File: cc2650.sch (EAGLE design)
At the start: 23 parts, among them IC4 CC2650MODAMOHR, SW1 SPST_TACT-KMR2, SW2 SPST_TACT-KMR2, U402 TPS62237DRY

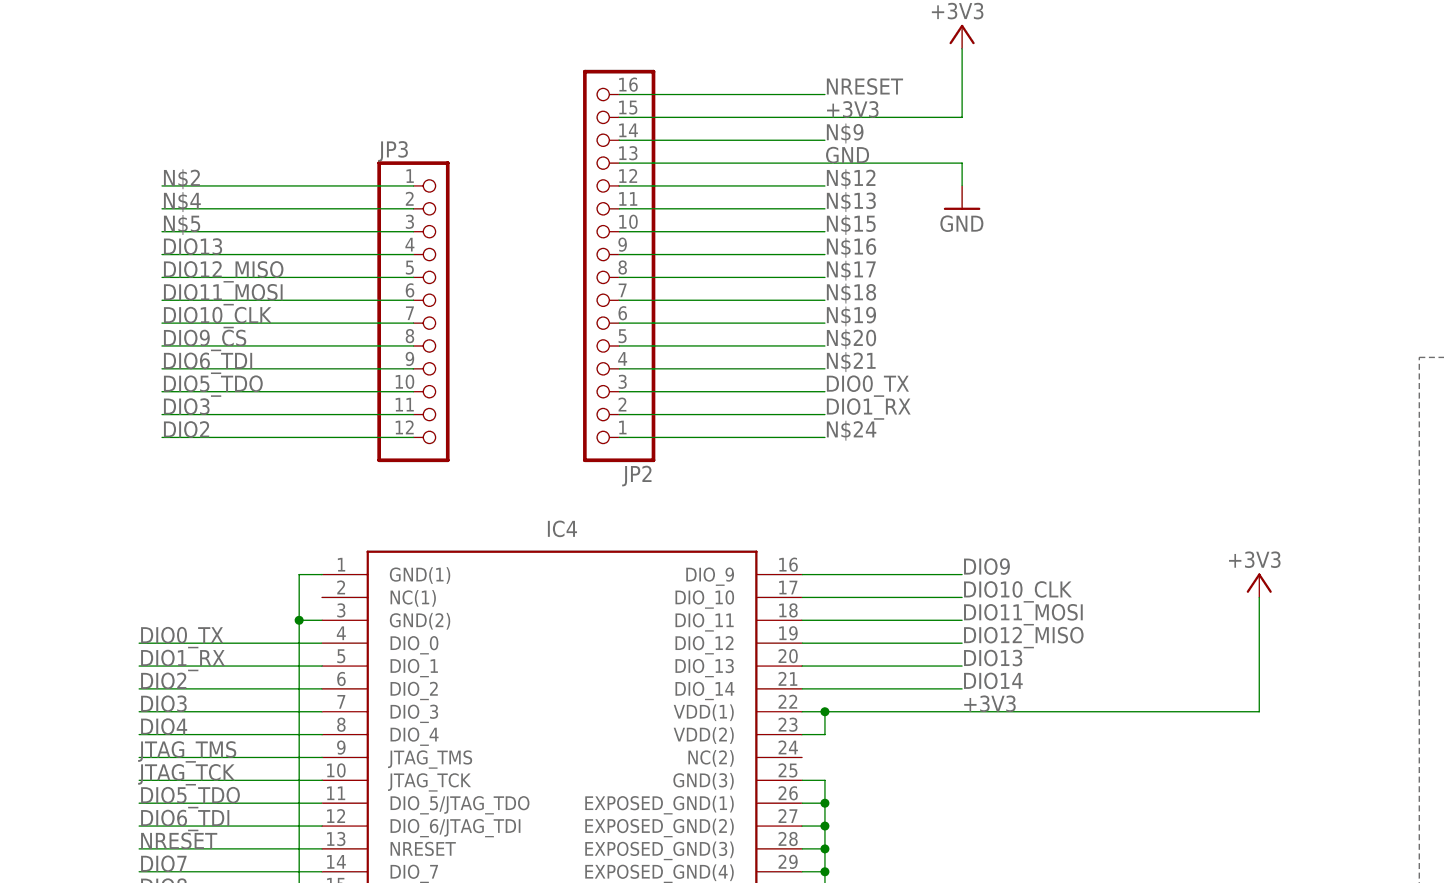
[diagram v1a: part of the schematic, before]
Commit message: changed pinout.
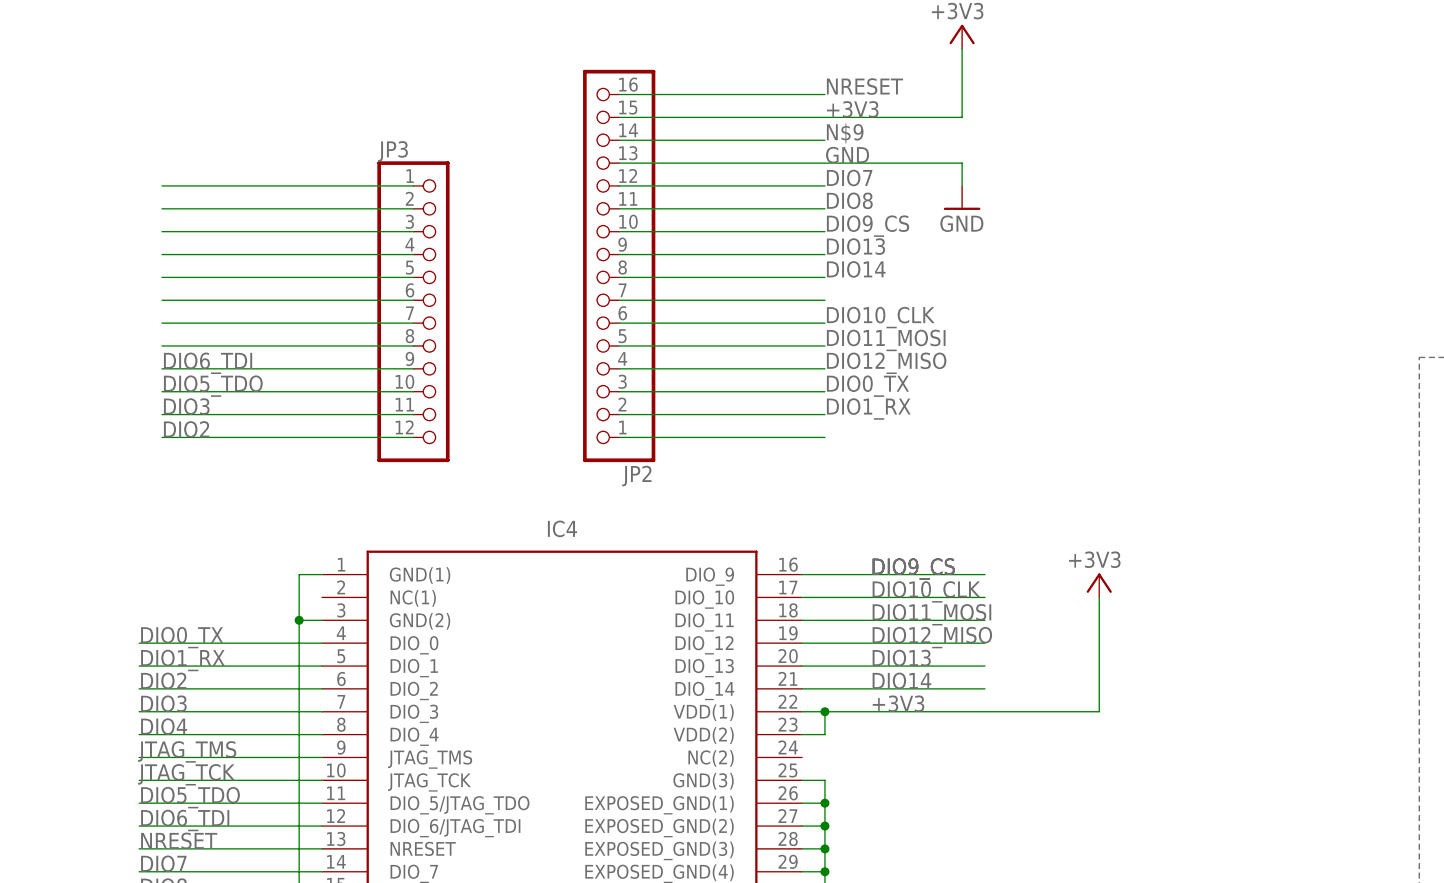
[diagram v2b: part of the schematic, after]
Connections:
- removed net DIO9: IC4.DIO_9
- removed net N$1: IC4.DIO_10
- removed net N$12: JP2.12
- removed net N$13: JP2.11
- removed net N$15: JP2.10
- removed net N$16: JP2.9
- removed net N$17: JP2.8
- removed net N$19: JP2.6
- removed net N$20: JP2.5
- removed net N$21: JP2.4
- net DIO10_CLK: now also IC4.DIO_10, JP2.6
- net DIO11_MOSI: now also JP2.5
- net DIO12_MISO: now also JP2.4
- net DIO13: now also JP2.9
- net DIO14: now also JP2.8
- net DIO7: now also JP2.12
- net DIO8: now also JP2.11
- net DIO9_CS: now also IC4.DIO_9, JP2.10
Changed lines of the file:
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@@
 <instance part="D1" gate="G$1" x="53.34" y="-10.16" rot="R90"/>
 <instance part="GND4" gate="1" x="35.56" y="-30.48"/>
-<instance part="+3V6" gate="G$1" x="0" y="7.62" smashed="yes">
-<attribute name="VALUE" x="2.54" y="10.16" size="1.778" layer="96" rot="R180"/>
+<instance part="+3V6" gate="G$1" x="-17.78" y="7.62" smashed="yes">
+<attribute name="VALUE" x="-15.24" y="10.16" size="1.778" layer="96" rot="R180"/>
 </instance>
 <instance part="GND5" gate="1" x="93.98" y="-76.2"/>
@@
 <segment>
 <pinref part="+3V6" gate="G$1" pin="+3V3"/>
-<wire x1="0" y1="5.08" x2="0" y2="-7.62" width="0.1524" layer="91"/>
+<wire x1="-17.78" y1="5.08" x2="-17.78" y2="-7.62" width="0.1524" layer="91"/>
 <pinref part="IC4" gate="G$1" pin="VDD(1)"/>
-<wire x1="0" y1="-7.62" x2="-48.26" y2="-7.62" width="0.1524" layer="91"/>
+<wire x1="-17.78" y1="-7.62" x2="-48.26" y2="-7.62" width="0.1524" layer="91"/>
 <pinref part="IC4" gate="G$1" pin="VDD(2)"/>
 <wire x1="-48.26" y1="-7.62" x2="-50.8" y2="-7.62" width="0.1524" layer="91"/>
@@
 <wire x1="-48.26" y1="-10.16" x2="-48.26" y2="-7.62" width="0.1524" layer="91"/>
 <junction x="-48.26" y="-7.62"/>
-<label x="-33.02" y="-7.62" size="1.778" layer="95"/>
+<label x="-43.18" y="-7.62" size="1.778" layer="95"/>
 </segment>
 <segment>
@@
 <label x="-124.46" y="-25.4" size="1.778" layer="95"/>
 </segment>
+<segment>
+<pinref part="JP2" gate="A" pin="12"/>
+<wire x1="-71.12" y1="50.8" x2="-48.26" y2="50.8" width="0.1524" layer="91"/>
+<label x="-48.26" y="50.8" size="1.778" layer="95"/>
+</segment>
 </net>
 <net name="DIO0_TX" class="0">
@@
 <net name="DIO10_CLK" class="0">
 <segment>
-<label x="-33.02" y="5.08" size="1.778" layer="95"/>
-</segment>
-<segment>
 <pinref part="JP3" gate="G$1" pin="7"/>
 <wire x1="-93.98" y1="35.56" x2="-121.92" y2="35.56" width="0.1524" layer="91"/>
-<label x="-121.92" y="35.56" size="1.778" layer="95"/>
+</segment>
+<segment>
+<pinref part="IC4" gate="G$1" pin="DIO_10"/>
+<wire x1="-50.8" y1="5.08" x2="-30.48" y2="5.08" width="0.1524" layer="91"/>
+<label x="-43.18" y="5.08" size="1.778" layer="95"/>
+</segment>
+<segment>
+<pinref part="JP2" gate="A" pin="6"/>
+<wire x1="-71.12" y1="35.56" x2="-48.26" y2="35.56" width="0.1524" layer="91"/>
+<label x="-48.26" y="35.56" size="1.778" layer="95"/>
 </segment>
 </net>
@@
 <pinref part="JP3" gate="G$1" pin="8"/>
 <wire x1="-93.98" y1="33.02" x2="-121.92" y2="33.02" width="0.1524" layer="91"/>
-<label x="-121.92" y="33.02" size="1.778" layer="95"/>
+</segment>
+<segment>
+<pinref part="IC4" gate="G$1" pin="DIO_9"/>
+<wire x1="-50.8" y1="7.62" x2="-30.48" y2="7.62" width="0.1524" layer="91"/>
+<label x="-43.18" y="7.62" size="1.778" layer="95"/>
+<label x="-43.18" y="7.62" size="1.778" layer="95"/>
+</segment>
+<segment>
+<pinref part="JP2" gate="A" pin="10"/>
+<wire x1="-71.12" y1="45.72" x2="-48.26" y2="45.72" width="0.1524" layer="91"/>
+<label x="-48.26" y="45.72" size="1.778" layer="95"/>
 </segment>
 </net>
@@
 <segment>
 <pinref part="IC4" gate="G$1" pin="DIO_12"/>
-<wire x1="-33.02" y1="0" x2="-50.8" y2="0" width="0.1524" layer="91"/>
-<label x="-33.02" y="0" size="1.778" layer="95"/>
+<wire x1="-30.48" y1="0" x2="-50.8" y2="0" width="0.1524" layer="91"/>
+<label x="-43.18" y="0" size="1.778" layer="95"/>
 </segment>
 <segment>
 <pinref part="JP3" gate="G$1" pin="5"/>
 <wire x1="-93.98" y1="40.64" x2="-121.92" y2="40.64" width="0.1524" layer="91"/>
-<label x="-121.92" y="40.64" size="1.778" layer="95"/>
+</segment>
+<segment>
+<pinref part="JP2" gate="A" pin="4"/>
+<wire x1="-71.12" y1="30.48" x2="-48.26" y2="30.48" width="0.1524" layer="91"/>
+<label x="-48.26" y="30.48" size="1.778" layer="95"/>
 </segment>
 </net>
@@
 <segment>
 <pinref part="IC4" gate="G$1" pin="DIO_13"/>
-<wire x1="-50.8" y1="-2.54" x2="-33.02" y2="-2.54" width="0.1524" layer="91"/>
-<label x="-33.02" y="-2.54" size="1.778" layer="95"/>
+<wire x1="-50.8" y1="-2.54" x2="-30.48" y2="-2.54" width="0.1524" layer="91"/>
+<label x="-43.18" y="-2.54" size="1.778" layer="95"/>
 </segment>
 <segment>
 <pinref part="JP3" gate="G$1" pin="4"/>
 <wire x1="-93.98" y1="43.18" x2="-121.92" y2="43.18" width="0.1524" layer="91"/>
-<label x="-121.92" y="43.18" size="1.778" layer="95"/>
+</segment>
+<segment>
+<pinref part="JP2" gate="A" pin="9"/>
+<wire x1="-71.12" y1="43.18" x2="-48.26" y2="43.18" width="0.1524" layer="91"/>
+<label x="-48.26" y="43.18" size="1.778" layer="95"/>
 </segment>
 </net>
@@
 <segment>
 <pinref part="IC4" gate="G$1" pin="DIO_14"/>
-<wire x1="-33.02" y1="-5.08" x2="-50.8" y2="-5.08" width="0.1524" layer="91"/>
-<label x="-33.02" y="-5.08" size="1.778" layer="95"/>
+<wire x1="-30.48" y1="-5.08" x2="-50.8" y2="-5.08" width="0.1524" layer="91"/>
+<label x="-43.18" y="-5.08" size="1.778" layer="95"/>
+</segment>
+<segment>
+<pinref part="JP2" gate="A" pin="8"/>
+<wire x1="-71.12" y1="40.64" x2="-48.26" y2="40.64" width="0.1524" layer="91"/>
+<label x="-48.26" y="40.64" size="1.778" layer="95"/>
 </segment>
 </net>
@@
 </segment>
 </net>
-<net name="N$1" class="0">
-<segment>
-<pinref part="IC4" gate="G$1" pin="DIO_10"/>
-<wire x1="-50.8" y1="5.08" x2="-33.02" y2="5.08" width="0.1524" layer="91"/>
-</segment>
-</net>
 <net name="DIO11_MOSI" class="0">
 <segment>
 <pinref part="IC4" gate="G$1" pin="DIO_11"/>
-<wire x1="-33.02" y1="2.54" x2="-50.8" y2="2.54" width="0.1524" layer="91"/>
-<label x="-33.02" y="2.54" size="1.778" layer="95"/>
+<wire x1="-30.48" y1="2.54" x2="-50.8" y2="2.54" width="0.1524" layer="91"/>
+<label x="-43.18" y="2.54" size="1.778" layer="95"/>
 </segment>
 <segment>
 <pinref part="JP3" gate="G$1" pin="6"/>
 <wire x1="-93.98" y1="38.1" x2="-121.92" y2="38.1" width="0.1524" layer="91"/>
-<label x="-121.92" y="38.1" size="1.778" layer="95"/>
-</segment>
-</net>
-<net name="DIO9" class="0">
-<segment>
-<pinref part="IC4" gate="G$1" pin="DIO_9"/>
-<wire x1="-50.8" y1="7.62" x2="-33.02" y2="7.62" width="0.1524" layer="91"/>
-<label x="-33.02" y="7.62" size="1.778" layer="95"/>
+</segment>
+<segment>
+<pinref part="JP2" gate="A" pin="5"/>
+<wire x1="-71.12" y1="33.02" x2="-48.26" y2="33.02" width="0.1524" layer="91"/>
+<label x="-48.26" y="33.02" size="1.778" layer="95"/>
 </segment>
 </net>
@@
 <pinref part="JP3" gate="G$1" pin="1"/>
 <wire x1="-93.98" y1="50.8" x2="-121.92" y2="50.8" width="0.1524" layer="91"/>
-<label x="-121.92" y="50.8" size="1.778" layer="95"/>
 </segment>
 </net>
@@
 <pinref part="JP3" gate="G$1" pin="2"/>
 <wire x1="-93.98" y1="48.26" x2="-121.92" y2="48.26" width="0.1524" layer="91"/>
-<label x="-121.92" y="48.26" size="1.778" layer="95"/>
 </segment>
 </net>
@@
 <pinref part="JP3" gate="G$1" pin="3"/>
 <wire x1="-93.98" y1="45.72" x2="-121.92" y2="45.72" width="0.1524" layer="91"/>
-<label x="-121.92" y="45.72" size="1.778" layer="95"/>
 </segment>
 </net>
@@
 <label x="-124.46" y="-27.94" size="1.778" layer="95"/>
 </segment>
+<segment>
+<pinref part="JP2" gate="A" pin="11"/>
+<wire x1="-71.12" y1="48.26" x2="-48.26" y2="48.26" width="0.1524" layer="91"/>
+<label x="-48.26" y="48.26" size="1.778" layer="95"/>
+</segment>
 </net>
 <net name="N$9" class="0">
@@
 </segment>
 </net>
-<net name="N$12" class="0">
-<segment>
-<pinref part="JP2" gate="A" pin="12"/>
-<wire x1="-71.12" y1="50.8" x2="-48.26" y2="50.8" width="0.1524" layer="91"/>
-<label x="-48.26" y="50.8" size="1.778" layer="95"/>
-</segment>
-</net>
-<net name="N$13" class="0">
-<segment>
-<pinref part="JP2" gate="A" pin="11"/>
-<wire x1="-71.12" y1="48.26" x2="-48.26" y2="48.26" width="0.1524" layer="91"/>
-<label x="-48.26" y="48.26" size="1.778" layer="95"/>
-</segment>
-</net>
-<net name="N$15" class="0">
-<segment>
-<pinref part="JP2" gate="A" pin="10"/>
-<wire x1="-71.12" y1="45.72" x2="-48.26" y2="45.72" width="0.1524" layer="91"/>
-<label x="-48.26" y="45.72" size="1.778" layer="95"/>
-</segment>
-</net>
-<net name="N$16" class="0">
-<segment>
-<pinref part="JP2" gate="A" pin="9"/>
-<wire x1="-71.12" y1="43.18" x2="-48.26" y2="43.18" width="0.1524" layer="91"/>
-<label x="-48.26" y="43.18" size="1.778" layer="95"/>
-</segment>
-</net>
-<net name="N$17" class="0">
-<segment>
-<pinref part="JP2" gate="A" pin="8"/>
-<wire x1="-71.12" y1="40.64" x2="-48.26" y2="40.64" width="0.1524" layer="91"/>
-<label x="-48.26" y="40.64" size="1.778" layer="95"/>
-</segment>
-</net>
 <net name="N$18" class="0">
 <segment>
 <pinref part="JP2" gate="A" pin="7"/>
 <wire x1="-71.12" y1="38.1" x2="-48.26" y2="38.1" width="0.1524" layer="91"/>
-<label x="-48.26" y="38.1" size="1.778" layer="95"/>
-</segment>
-</net>
-<net name="N$19" class="0">
-<segment>
-<pinref part="JP2" gate="A" pin="6"/>
-<wire x1="-71.12" y1="35.56" x2="-48.26" y2="35.56" width="0.1524" layer="91"/>
-<label x="-48.26" y="35.56" size="1.778" layer="95"/>
-</segment>
-</net>
-<net name="N$20" class="0">
-<segment>
-<pinref part="JP2" gate="A" pin="5"/>
-<wire x1="-71.12" y1="33.02" x2="-48.26" y2="33.02" width="0.1524" layer="91"/>
-<label x="-48.26" y="33.02" size="1.778" layer="95"/>
-</segment>
-</net>
-<net name="N$21" class="0">
-<segment>
-<pinref part="JP2" gate="A" pin="4"/>
-<wire x1="-71.12" y1="30.48" x2="-48.26" y2="30.48" width="0.1524" layer="91"/>
-<label x="-48.26" y="30.48" size="1.778" layer="95"/>
 </segment>
 </net>
@@
 <pinref part="JP2" gate="A" pin="1"/>
 <wire x1="-71.12" y1="22.86" x2="-48.26" y2="22.86" width="0.1524" layer="91"/>
-<label x="-48.26" y="22.86" size="1.778" layer="95"/>
-</segment>
-</net>
+</segment>
+</net>

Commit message: changed pinout and added second routing path.
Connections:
- removed net N$18: JP2.7
- removed net N$2: JP3.1
- removed net N$24: JP2.1
- removed net N$4: JP3.2
- removed net N$5: JP3.3
- removed net N$9: JP2.14
- net DIO10_CLK: no longer JP3.7
- net DIO11_MOSI: no longer JP3.6
- net DIO12_MISO: no longer JP3.5
- net DIO13: no longer JP3.4
- net DIO9_CS: no longer JP3.8
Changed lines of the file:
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@@
 <net name="DIO10_CLK" class="0">
-<segment>
-<pinref part="JP3" gate="G$1" pin="7"/>
-<wire x1="-93.98" y1="35.56" x2="-121.92" y2="35.56" width="0.1524" layer="91"/>
-</segment>
 <segment>
 <pinref part="IC4" gate="G$1" pin="DIO_10"/>
@@
 <net name="DIO9_CS" class="0">
 <segment>
-<pinref part="JP3" gate="G$1" pin="8"/>
-<wire x1="-93.98" y1="33.02" x2="-121.92" y2="33.02" width="0.1524" layer="91"/>
-</segment>
-<segment>
 <pinref part="IC4" gate="G$1" pin="DIO_9"/>
 <wire x1="-50.8" y1="7.62" x2="-30.48" y2="7.62" width="0.1524" layer="91"/>
@@
 </segment>
 <segment>
-<pinref part="JP3" gate="G$1" pin="5"/>
-<wire x1="-93.98" y1="40.64" x2="-121.92" y2="40.64" width="0.1524" layer="91"/>
-</segment>
-<segment>
 <pinref part="JP2" gate="A" pin="4"/>
 <wire x1="-71.12" y1="30.48" x2="-48.26" y2="30.48" width="0.1524" layer="91"/>
@@
 <wire x1="-50.8" y1="-2.54" x2="-30.48" y2="-2.54" width="0.1524" layer="91"/>
 <label x="-43.18" y="-2.54" size="1.778" layer="95"/>
-</segment>
-<segment>
-<pinref part="JP3" gate="G$1" pin="4"/>
-<wire x1="-93.98" y1="43.18" x2="-121.92" y2="43.18" width="0.1524" layer="91"/>
 </segment>
 <segment>
@@
 </segment>
 <segment>
-<pinref part="JP3" gate="G$1" pin="6"/>
-<wire x1="-93.98" y1="38.1" x2="-121.92" y2="38.1" width="0.1524" layer="91"/>
-</segment>
-<segment>
 <pinref part="JP2" gate="A" pin="5"/>
 <wire x1="-71.12" y1="33.02" x2="-48.26" y2="33.02" width="0.1524" layer="91"/>
 <label x="-48.26" y="33.02" size="1.778" layer="95"/>
-</segment>
-</net>
-<net name="N$2" class="0">
-<segment>
-<pinref part="JP3" gate="G$1" pin="1"/>
-<wire x1="-93.98" y1="50.8" x2="-121.92" y2="50.8" width="0.1524" layer="91"/>
-</segment>
-</net>
-<net name="N$4" class="0">
-<segment>
-<pinref part="JP3" gate="G$1" pin="2"/>
-<wire x1="-93.98" y1="48.26" x2="-121.92" y2="48.26" width="0.1524" layer="91"/>
-</segment>
-</net>
-<net name="N$5" class="0">
-<segment>
-<pinref part="JP3" gate="G$1" pin="3"/>
-<wire x1="-93.98" y1="45.72" x2="-121.92" y2="45.72" width="0.1524" layer="91"/>
 </segment>
 </net>
@@
 </segment>
 </net>
-<net name="N$9" class="0">
-<segment>
-<pinref part="JP2" gate="A" pin="14"/>
-<wire x1="-71.12" y1="55.88" x2="-48.26" y2="55.88" width="0.1524" layer="91"/>
-<label x="-48.26" y="55.88" size="1.778" layer="95"/>
-</segment>
-</net>
-<net name="N$18" class="0">
-<segment>
-<pinref part="JP2" gate="A" pin="7"/>
-<wire x1="-71.12" y1="38.1" x2="-48.26" y2="38.1" width="0.1524" layer="91"/>
-</segment>
-</net>
-<net name="N$24" class="0">
-<segment>
-<pinref part="JP2" gate="A" pin="1"/>
-<wire x1="-71.12" y1="22.86" x2="-48.26" y2="22.86" width="0.1524" layer="91"/>
-</segment>
-</net>

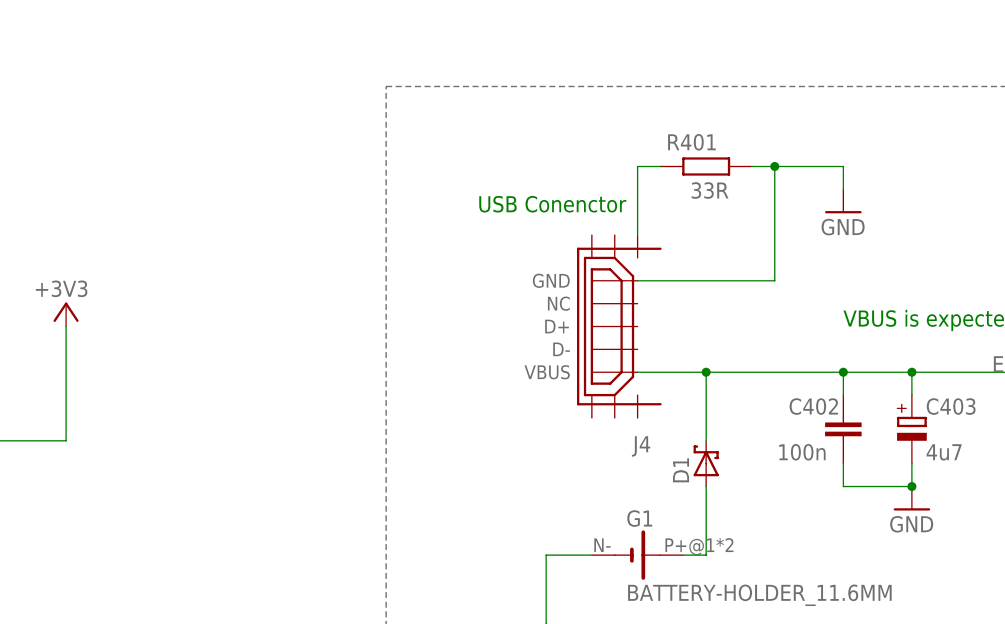
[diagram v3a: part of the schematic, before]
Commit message: changed usb connector
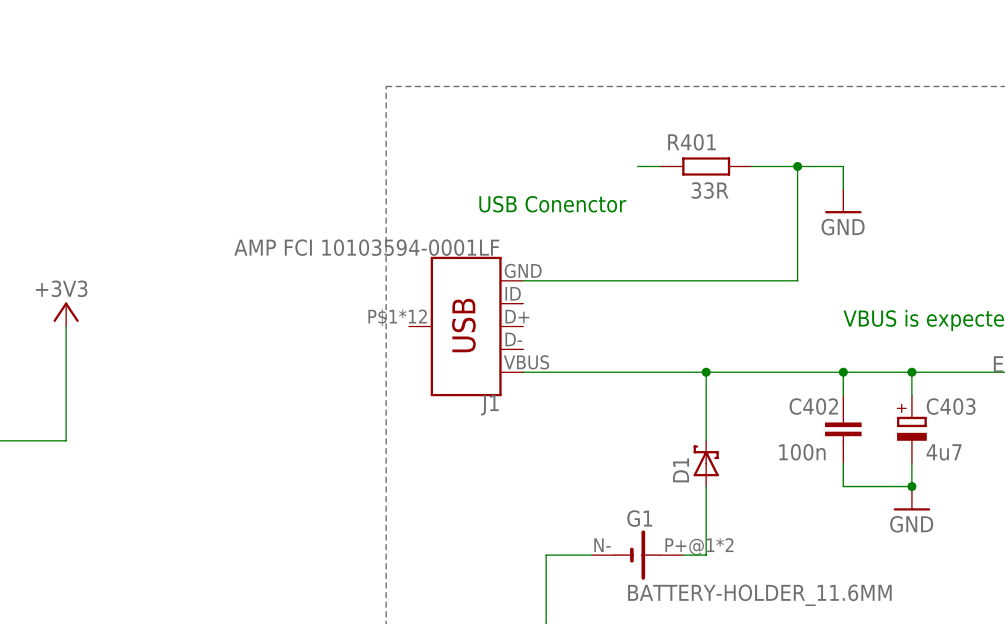
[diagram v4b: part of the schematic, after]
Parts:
- removed J4: (no value), usb_con-update:USB_MICRO_FLIPPED
- added J1: AMP FCI 10103594-0001LF, SparkFun-Connectors:USB_MICRO-B_HALF_PTH
- C17: MPN (none) -> EVQ-Q2F03W; OC_NEWARK (none) -> 96K9626
- C401, C402, C403, C404, D1, D2, G1, IC4, JP1, JP2, JP3, JP8, JTAG_CONNECTOR, L401, LED3, R27, R29, R401, SW1, SW2, U402: OC_NEWARK (none) -> unknown
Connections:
- net EZFET_VBUS: now also J1.VBUS; no longer J4.VBUS
- net GND: now also J1.GND; no longer J4.GND
- net N$10: no longer J4.SHIELD1
